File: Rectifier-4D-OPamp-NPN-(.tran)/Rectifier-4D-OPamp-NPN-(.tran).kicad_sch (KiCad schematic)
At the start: 19 parts, among them Q1 BDX53C, U1 LM741

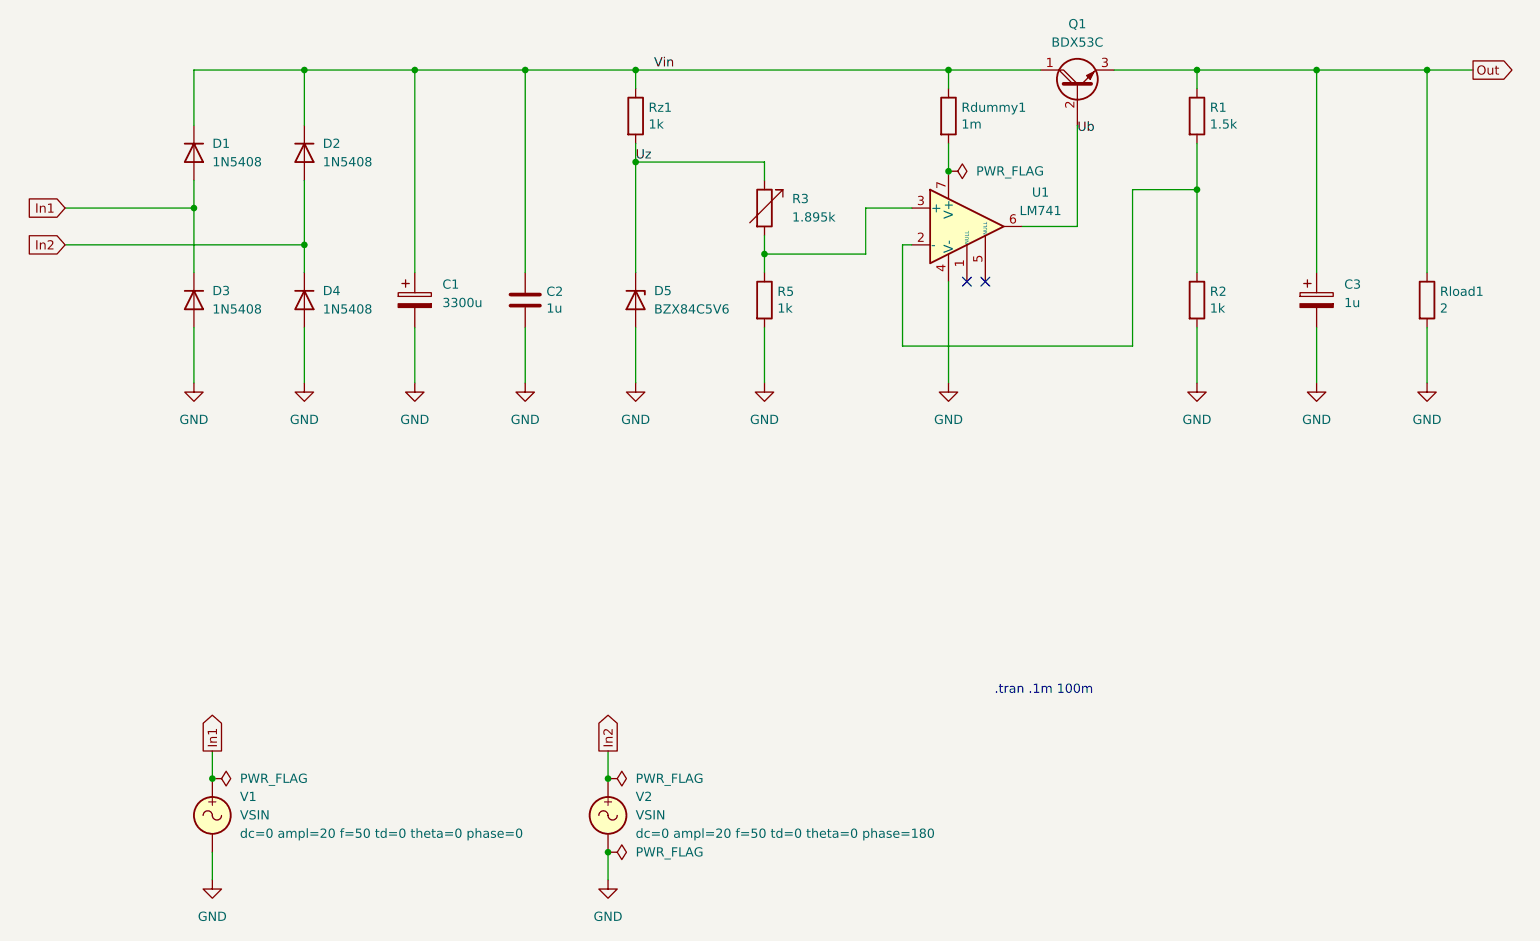
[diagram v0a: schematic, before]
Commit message: Updated all schematics and prepared for KiCad 8.0
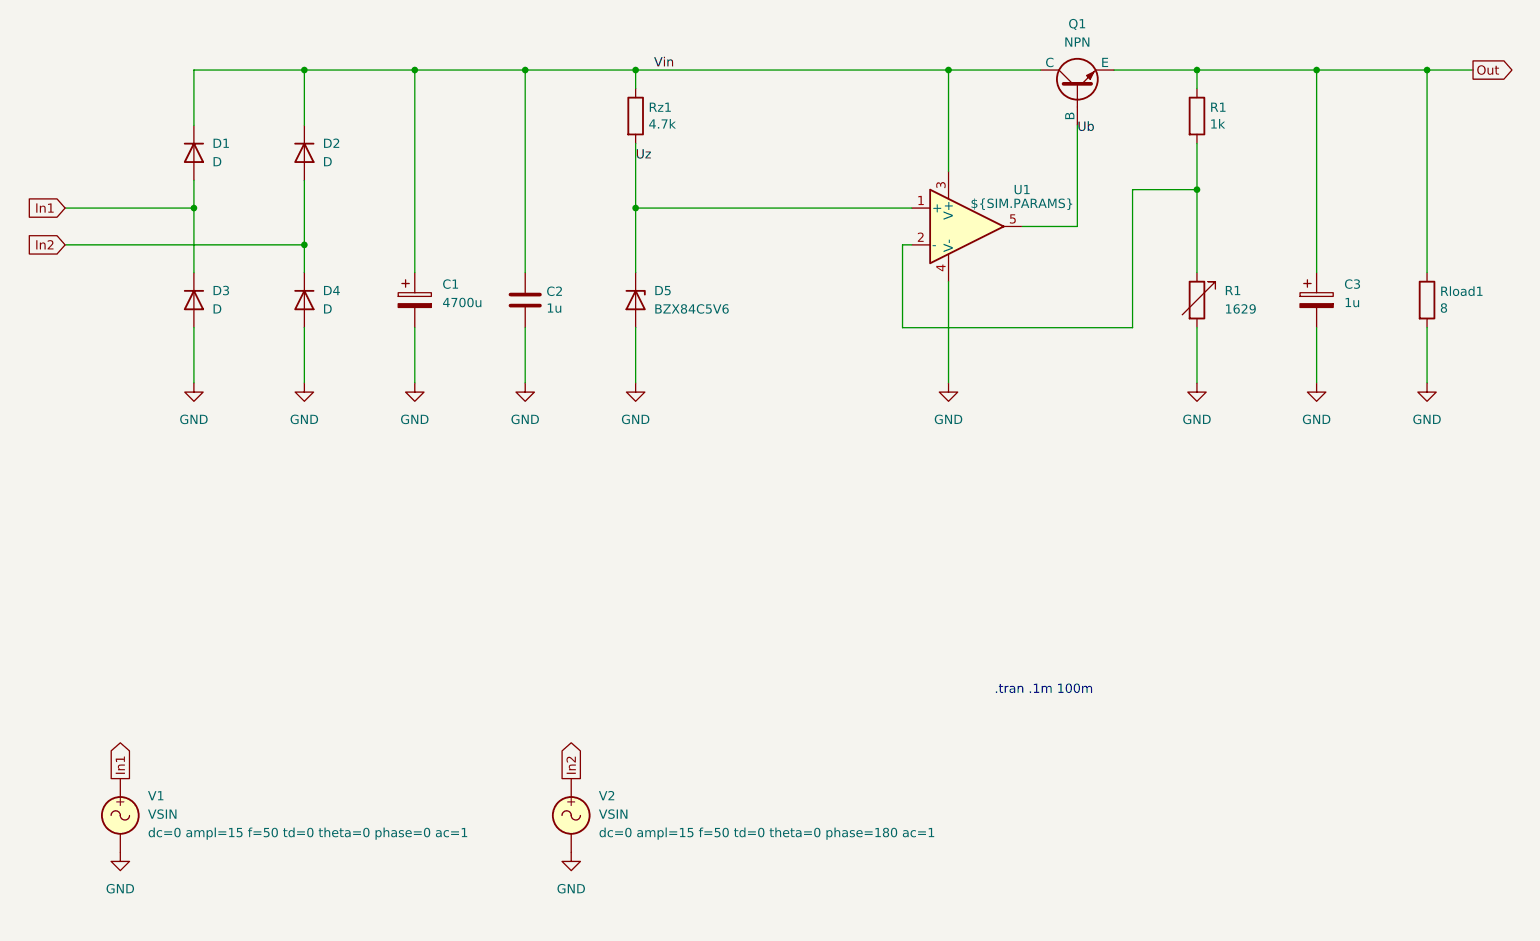
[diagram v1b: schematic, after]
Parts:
- removed Q1: BDX53C, symbol Device:Q_NPN_Darlington_CBE
- removed R2, R5: 1k, Resistor_THT:R_Axial_DIN0309_L9.0mm_D3.2mm_P12.70mm_Horizontal, symbol Device:R
- removed R3: 1.895k, symbol Device:R_Variable
- removed Rdummy1: 1m, Resistor_THT:R_Axial_DIN0309_L9.0mm_D3.2mm_P12.70mm_Horizontal, symbol Device:R
- removed U1: LM741, symbol Amplifier_Operational:LM741
- added Q1: NPN, symbol Simulation_SPICE:NPN
- added R1: 1629, symbol Device:R_Variable
- added U1: ${SIM.PARAMS}, symbol Simulation_SPICE:OPAMP
- C1: value 3300u -> 4700u
- D1, D2, D3, D4: value 1N5408 -> D
- R1: value 1.5k -> 1k
- Rload1: value 2 -> 8
- Rz1: value 1k -> 4.7k
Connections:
- net GND: now also R1.2, U1.4 (V-)
- net Out: now also Q1.3 (E)
- net Ub: now also Q1.2 (B), U1.5
- net Uz: now also U1.1 (+)
- net Vin: now also Q1.1 (C), U1.3 (V+)
- net at R1.2: now also R1.1, U1.2 (-)
- no-connect marks 2 -> 0
